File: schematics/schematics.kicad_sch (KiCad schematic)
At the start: 12 parts, among them SW1 SW_Push, SW1 SW_SPDT, SW2 SW_Push, U1 LF33_TO220, U2 ESP32-C6-DevKitC-1

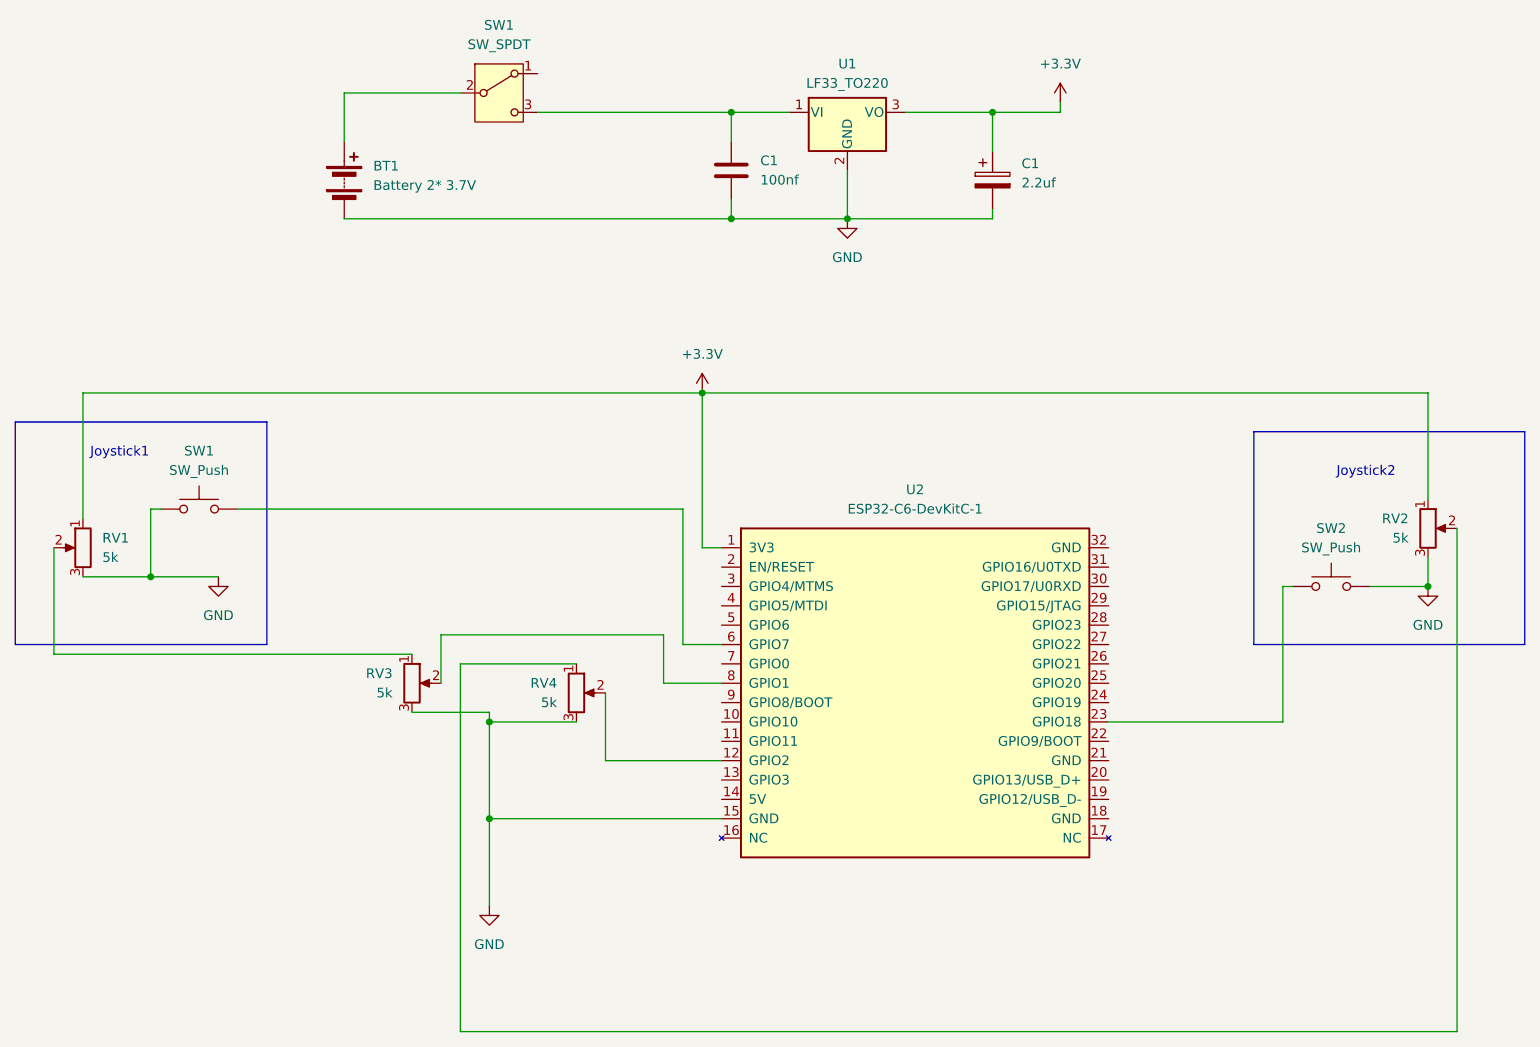
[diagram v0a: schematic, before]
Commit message: added capacitors to joysticks output lines
Signed-off-by: zayats1 <zaiats.bogdan@gmail.com>
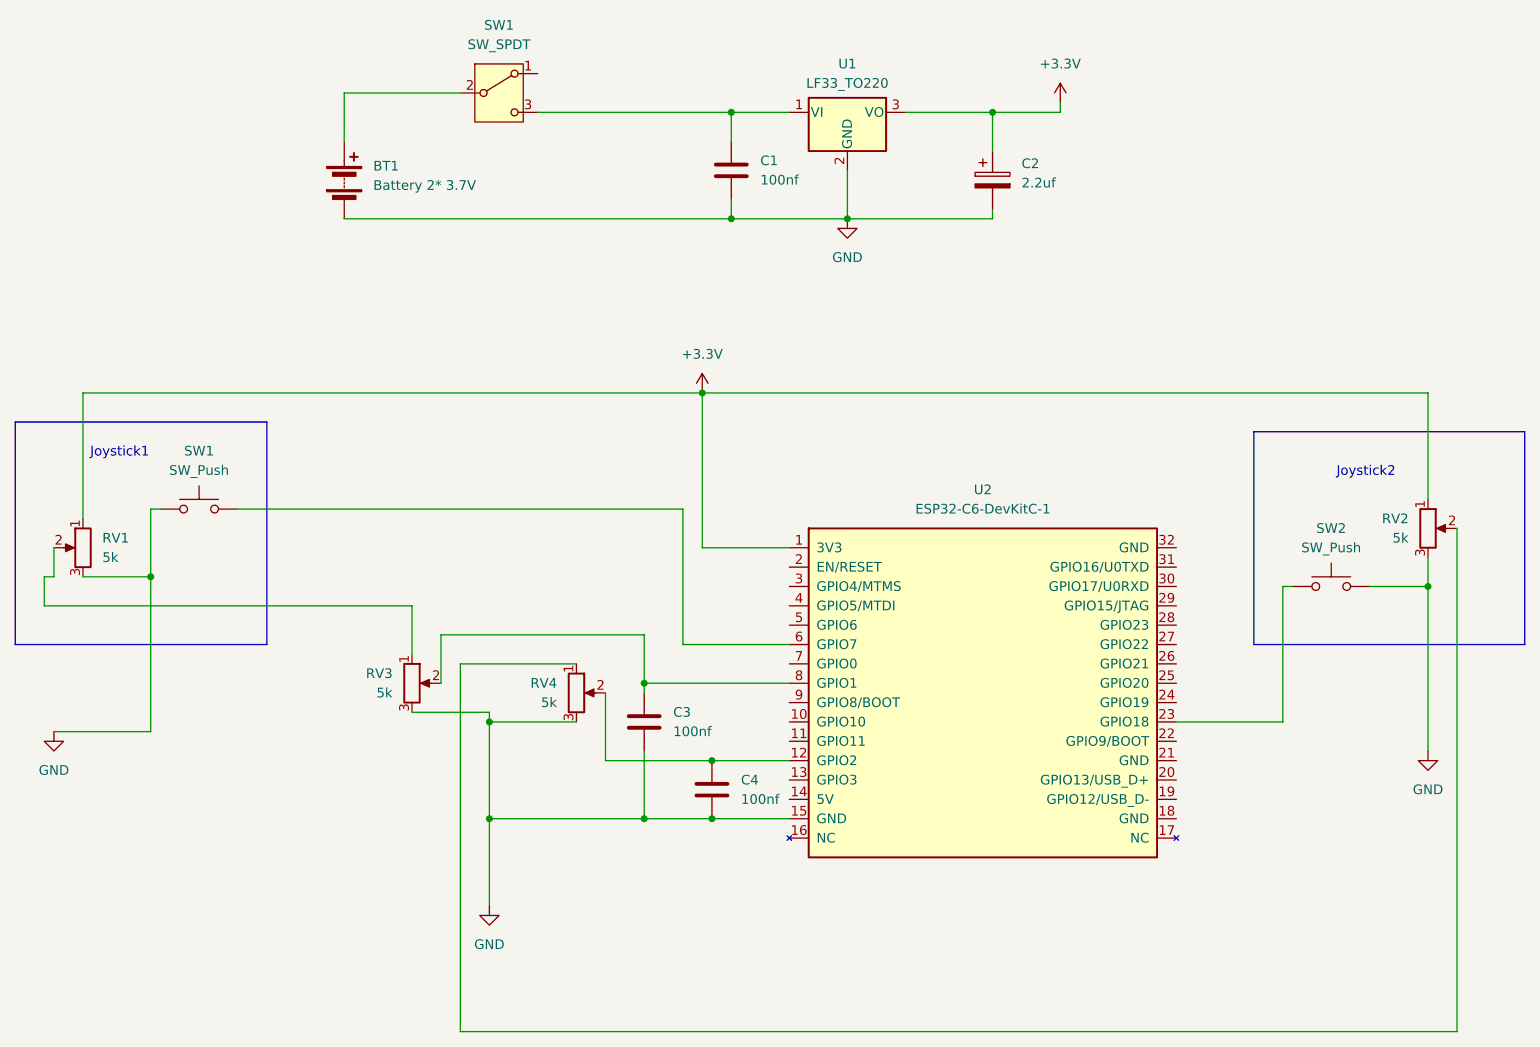
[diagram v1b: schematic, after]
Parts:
- added C3, C4: 100nf, symbol Device:C
- renumbered C1 to C2
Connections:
- net GND: now also C3.2, C4.2
- net at RV3.2, U2.8 (GPIO1): now also C3.1
- net at RV4.2, U2.12 (GPIO2): now also C4.1
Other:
- moved on the sheet: U2
